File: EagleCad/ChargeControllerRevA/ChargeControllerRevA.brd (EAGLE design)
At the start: 100 x 80 mm, 59 parts, among them Q1 SI7135DP, Q2 SI7135DP

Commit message: renamed RC
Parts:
- removed CC1, CC2, CVCC: (no value), rcl:C025-050X050
- removed R2, RC, RS1: (no value), rcl:0309/12
- removed VOUT(1): (no value), wirepad:3,81/1,4
- added C1, C4, C7: (no value), rcl:C025-050X050
- added R2', R21, R7: (no value), rcl:0309/12
- moved R3 51.0 mm to (19.1, 41.9), turned to 90 degrees
- moved C8 40.4 mm to (48.3, 49.5), turned to 90 degrees
- moved R11 38.8 mm to (67.3, 73.7), turned to 0 degrees
- moved R12 35.2 mm to (67.3, 69.8), turned to 180 degrees
- moved R1 35.1 mm to (3.81, 64.8)
- moved R8 31.4 mm to (41.9, 41.9), turned to 90 degrees
- moved R10 26.7 mm to (67.3, 77.5), turned to 180 degrees
- moved R9 22.5 mm to (52.1, 38.1), turned to 90 degrees
- moved R15 19.0 mm to (67.3, 58.4)
- moved R16 19.0 mm to (67.3, 54.6), turned to 180 degrees
- moved R17 19.0 mm to (67.3, 50.8), turned to 0 degrees
- moved CIN 17.3 mm to (8.89, 71.1), turned to 0 degrees
- moved CIN2 17.3 mm to (3.81, 54.6), turned to 270 degrees
- moved C2 17.0 mm to (24.1, 21.6), turned to 180 degrees
- moved R18 11.4 mm to (87.6, 48.3)
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- renumbered CF to C3, CIN1 to C10, CIN3 to C14, CIN4 to C13, CIN5 to C11, CIN6 to C12, COUT to C9, CSS to C6, RS2 to R14
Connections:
- net BATT: now also R18.1; no longer R20.1
- net GND: now also C2.2, C5.2, C8.2, R12.1, R20.1, R21.1, R3.2, R5.1, R7.2; no longer CC1.2, CC2.2, CVCC.2, R1.1, R11.1, R17.1, R18.1, R4.2, R5.2
- net N$10: now also R3.1; no longer R4.1
- net N$11: now also C4.1; no longer C5.1
- net N$12: now also R2'.1; no longer R8.1
- net N$13: now also C2.1; no longer CVCC.1
- net N$16: now also R8.2; no longer R6.2
- net N$19: now also R9.1; no longer R12.1
- net N$2: now also C7.1, R7.1; no longer C2.1, R5.1
- net N$20: now also C1.1; no longer C8.1
- net N$21: now also R15.2; no longer R3.2
- net N$28: now also R10.1, R11.2; no longer R15.1, R16.2
- net N$29: now also R11.1, R12.2; no longer R16.1, R17.2
- net N$3: now also C7.2, R8.1; no longer C2.2, R6.1
- net N$35: now also R20.2; no longer R11.2
- net N$36: now also R21.2; no longer R18.2
- net N$4: now also C5.1, R6.2, R9.2; no longer CC2.1, R12.2, RC.2
- net N$40: now also R16.1, R17.2; no longer R10.2, R9.1
- net N$41: now also R17.1, R18.2; no longer R10.1, R20.2
- net N$42: now also R15.1, R16.2; no longer R3.1, R9.2
- net N$5: now also C8.1, R6.1; no longer CC1.1, RC.1
- net N$7: now also R4.1, R5.2; no longer R1.2, R2.1
- net SW1: now also C4.2; no longer C5.2
- net SW2: now also C1.2; no longer C8.2
- net VIN: now also CIN2.1, R1.2, R2'.2; no longer CIN.1, R8.2, RS1.2
- net VIN+: now also CIN.1, R1.1, R10.2; no longer CIN2.1, R15.2, RS1.1
- net VOUT(1): now also R4.2; no longer R2.2, VOUT(1).1

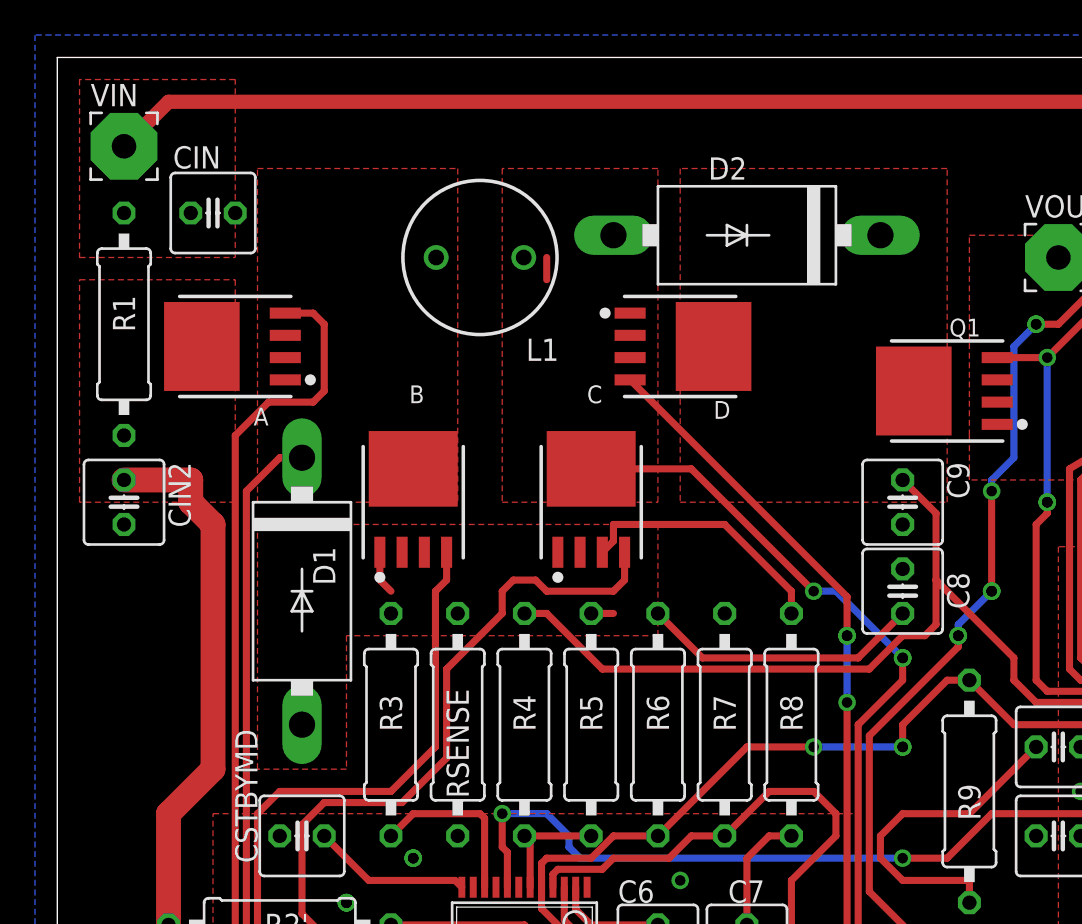
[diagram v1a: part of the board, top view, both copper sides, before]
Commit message: in/out caps added
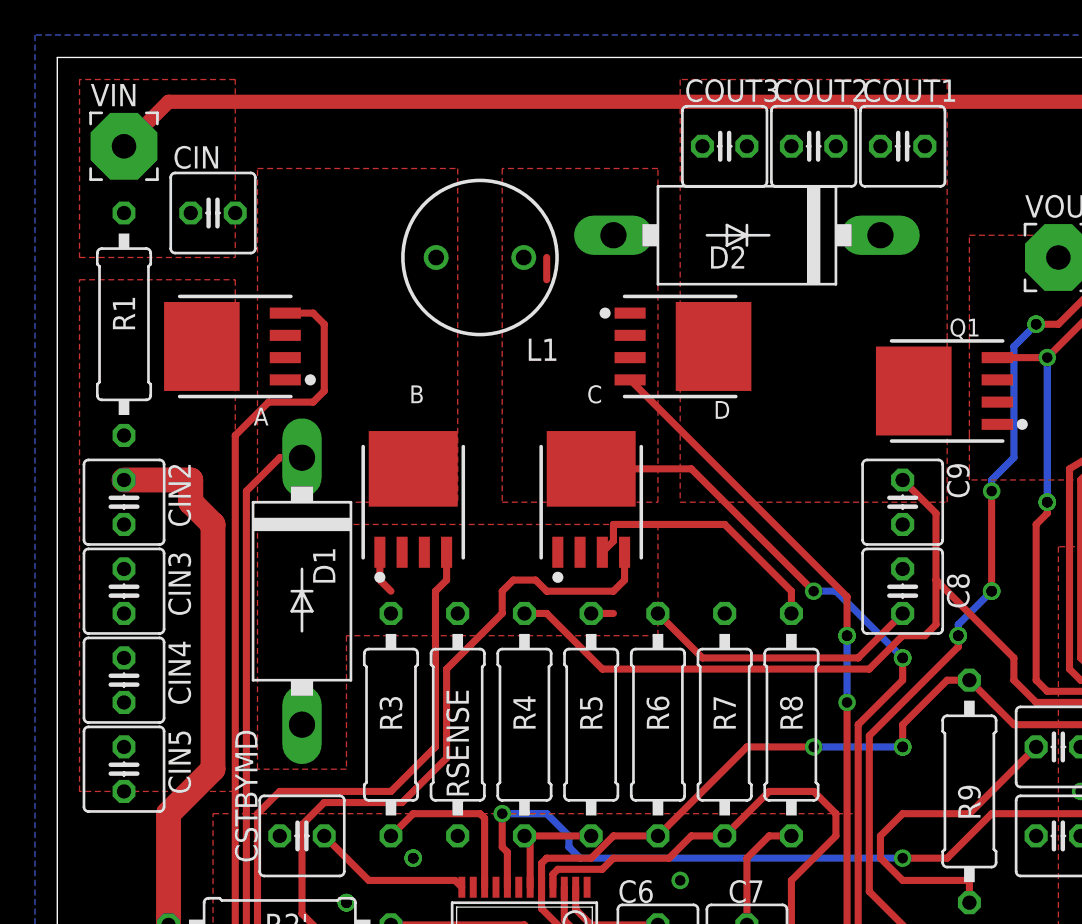
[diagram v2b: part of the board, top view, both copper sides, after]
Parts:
- added CIN3, CIN4, CIN5, COUT1, COUT2, COUT3: (no value), rcl:C025-050X050
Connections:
- net GND: now also CIN3.2, CIN4.2, CIN5.2, COUT1.2, COUT2.2, COUT3.2
- net VIN: now also CIN3.1, CIN4.1, CIN5.1
- net VOUT(1): now also COUT1.1, COUT2.1, COUT3.1
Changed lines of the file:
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@@
 </element>
 <element name="D2" library="diode" package="DO201-15" value="SB320" x="39.37" y="69.85" smashed="yes" rot="R180">
-<attribute name="NAME" x="39.37" y="74.295" size="1.27" layer="25" ratio="10" rot="R180"/>
+<attribute name="NAME" x="39.37" y="69.215" size="1.27" layer="25" ratio="10" rot="R180"/>
 <attribute name="VALUE" x="41.91" y="72.009" size="1.27" layer="27" ratio="10" rot="R180"/>
 </element>
@@
 <attribute name="VALUE" x="67.945" y="35.56" size="1.27" layer="27" rot="R90"/>
 </element>
+<element name="CIN5" library="rcl" package="C025-050X050" value="" x="3.81" y="39.37" rot="R270"/>
+<element name="CIN3" library="rcl" package="C025-050X050" value="" x="3.81" y="49.53" rot="R270"/>
+<element name="CIN4" library="rcl" package="C025-050X050" value="" x="3.81" y="44.45" rot="R270"/>
+<element name="COUT1" library="rcl" package="C025-050X050" value="" x="48.26" y="74.93"/>
+<element name="COUT2" library="rcl" package="C025-050X050" value="" x="43.18" y="74.93"/>
+<element name="COUT3" library="rcl" package="C025-050X050" value="" x="38.1" y="74.93"/>
 </elements>
 <signals>
@@
 <vertex x="35.56" y="54.61"/>
 <vertex x="50.8" y="54.61"/>
-<vertex x="50.8" y="73.66"/>
-<vertex x="35.56" y="73.66"/>
+<vertex x="50.8" y="78.74"/>
+<vertex x="35.56" y="78.74"/>
 </polygon>
 <wire x1="26.67" y1="48.26" x2="27.94" y2="48.26" width="0.4064" layer="1"/>
@@
 <contactref element="U$2" pad="PS19"/>
 <wire x1="64.8335" y1="40.9575" x2="60.6425" y2="40.9575" width="0.4064" layer="1"/>
+<contactref element="COUT2" pad="1"/>
+<contactref element="COUT1" pad="1"/>
+<contactref element="COUT3" pad="1"/>
 </signal>
 <signal name="N$10">
@@
 <polygon width="0.4064" layer="1">
 <vertex x="10.16" y="67.31"/>
-<vertex x="10.16" y="54.61"/>
-<vertex x="1.27" y="54.61"/>
+<vertex x="10.16" y="38.1"/>
+<vertex x="1.27" y="38.1"/>
 <vertex x="1.27" y="67.31"/>
 </polygon>
@@
 <contactref element="U$2" pad="PS22"/>
 <wire x1="64.8335" y1="39.0525" x2="61.9125" y2="39.0525" width="0.4064" layer="1"/>
+<contactref element="CIN5" pad="1"/>
+<contactref element="CIN3" pad="1"/>
+<contactref element="CIN4" pad="1"/>
 </signal>
 <signal name="N$14">
@@
 <contactref element="U$2" pad="PS6"/>
 <contactref element="U$2" pad="PS24"/>
+<contactref element="CIN5" pad="2"/>
+<contactref element="CIN4" pad="2"/>
+<contactref element="CIN3" pad="2"/>
+<contactref element="COUT1" pad="2"/>
+<contactref element="COUT2" pad="2"/>
+<contactref element="COUT3" pad="2"/>
 </signal>
 <signal name="SW1">
